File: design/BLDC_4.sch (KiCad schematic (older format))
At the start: 26 parts, among them K1 SERVO, P1 HALL/Encoder, P101 CANBUS, P3 PWR_COMM, P4 IN+, P5 IN-, P6 MOTOR1, P7 MOTOR2, P9 MOTOR3, X1 MINI-USB-SHIELD-32005-201

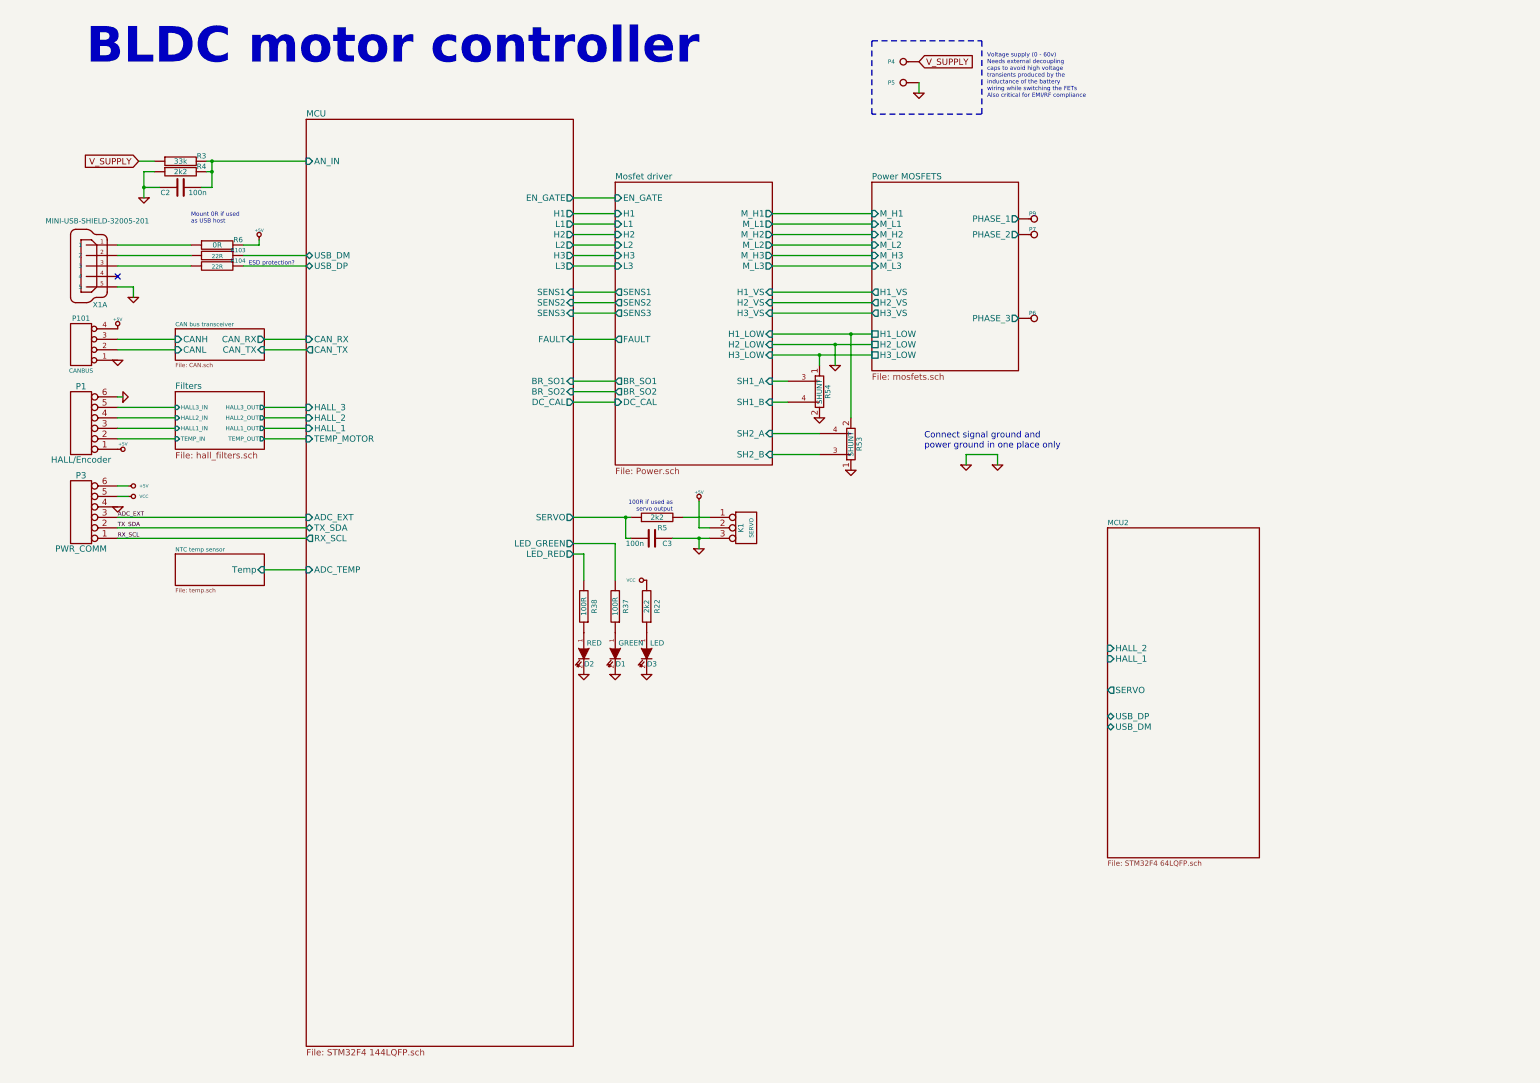
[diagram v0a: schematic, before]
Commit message: Add a electronic for second motor and add new pin's for it on MCU; TODO Add new mosfets
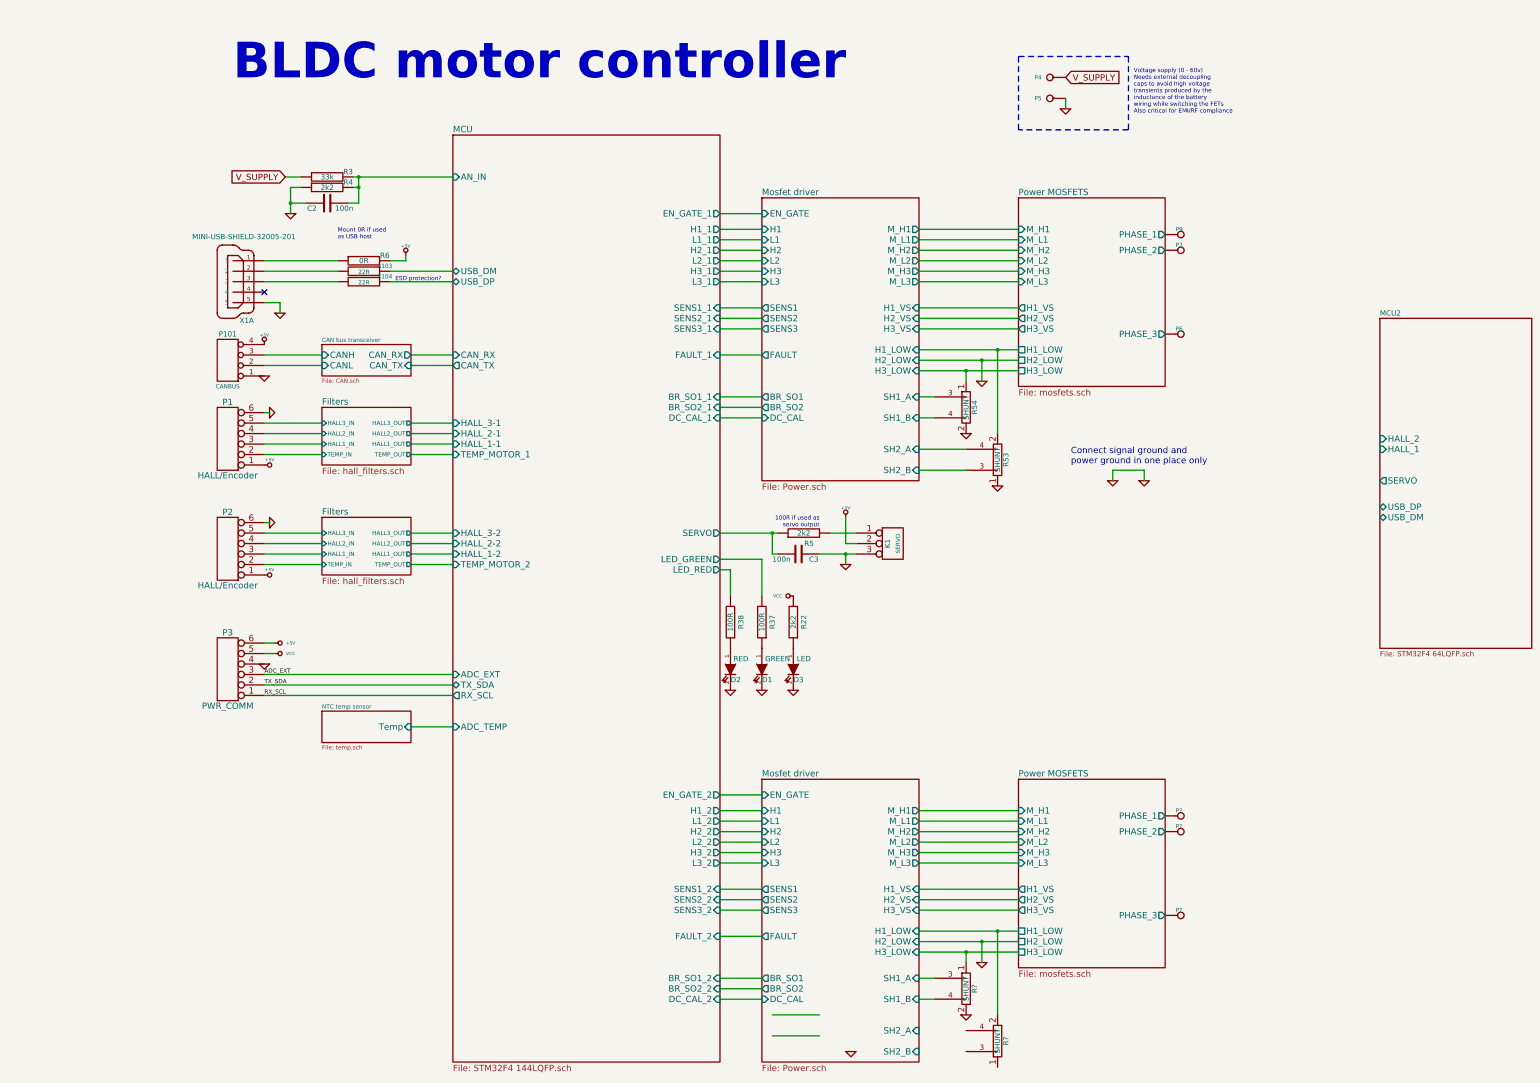
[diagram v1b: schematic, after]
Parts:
- added P2: HALL/Encoder, CRF1:MICRO_JST_6, symbol CONN_6
- added P?: MOTOR3, CRF1:1PAD_4x5mm, symbol CONN_1
- added P?: MOTOR2, CRF1:1PAD_4x5mm, symbol CONN_1
- added P?: MOTOR1, CRF1:1PAD_4x5mm, symbol CONN_1
- added R? (x2): SHUNT, CRF1:WSLP2726, symbol SHUNT
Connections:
- net +5V: now also P2.1
- net Filters/HALL1_IN: now also P2.3; no longer P1.3
- net Filters/HALL2_IN: now also P2.4; no longer P1.4
- net Filters/HALL3_IN: now also P2.5; no longer P1.5
- net Filters/TEMP_IN: now also P2.2; no longer P1.2
- net GND: now also P2.6, R?.2
- net Mosfet driver/H1_LOW: now also R?.2; no longer R53.2
- net Mosfet driver/H3_LOW: now also R?.1; no longer R54.1
- net Mosfet driver/SH1_A: now also R?.3; no longer R54.3
- net Mosfet driver/SH1_B: now also R?.4; no longer R54.4
- net Power MOSFETS/PHASE_1: now also P?.1; no longer P9.1
- net Power MOSFETS/PHASE_2: now also P?.1; no longer P7.1
- net Power MOSFETS/PHASE_3: now also P?.1; no longer P6.1
- new net Filters/HALL1_IN: P1.3
- new net Filters/HALL2_IN: P1.4
- new net Filters/HALL3_IN: P1.5
- new net Filters/TEMP_IN: P1.2
- new net Mosfet driver/H1_LOW: R53.2
- new net Mosfet driver/H3_LOW: R54.1
- new net Mosfet driver/SH1_A: R54.3
- new net Mosfet driver/SH1_B: R54.4
- new net Power MOSFETS/PHASE_1: P9.1
- new net Power MOSFETS/PHASE_2: P7.1
- new net Power MOSFETS/PHASE_3: P6.1
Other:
- moved on the sheet: C2, C3, D1, D2, D3, K1, P1, P101, P3, P4, P5, P6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

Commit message: Make change in annotations and some small fixes
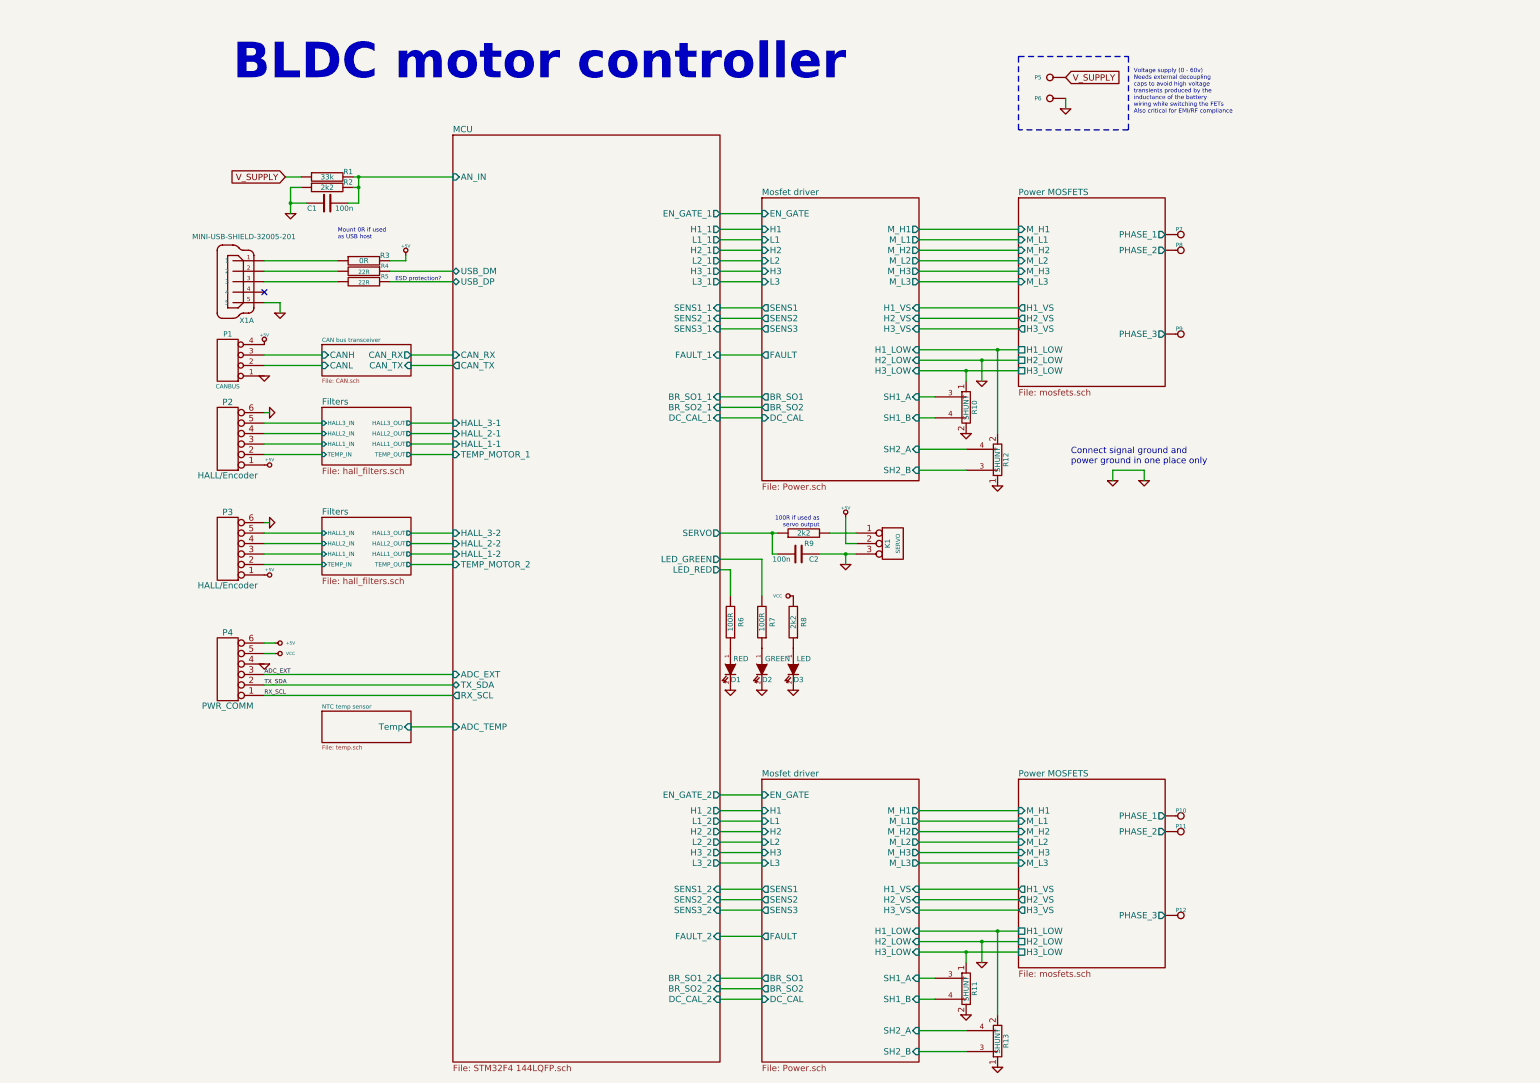
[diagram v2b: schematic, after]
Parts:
- gave numbers to parts that had none: 5
- renumbered C2 to C1, C3 to C2, D2 to D1, D1 to D2, P101 to P1, P1 to P2, P2 to P3, P3 to P4, P4 to P5, P5 to P6, P9 to P7, P7 to P8, P6 to P9, R3 to R1, R54 to R10, R53 to R12, R4 to R2, R6 to R3, R103 to R4, R104 to R5, R38 to R6, R37 to R7, R22 to R8, R5 to R9
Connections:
- net Filters/HALL1_IN is gone; now on net Filters/HALL1_IN: P3.3
- net Filters/HALL2_IN is gone; now on net Filters/HALL2_IN: P3.4
- net Filters/HALL3_IN is gone; now on net Filters/HALL3_IN: P3.5
- net Filters/TEMP_IN is gone; now on net Filters/TEMP_IN: P3.2
- net Mosfet driver/H1_LOW is gone; now on net Mosfet driver/H1_LOW: R13.2
- net Mosfet driver/H3_LOW is gone; now on net Mosfet driver/H3_LOW: R11.1
- net Mosfet driver/SH1_A is gone; now on net Mosfet driver/SH1_A: R11.3
- net Mosfet driver/SH1_B is gone; now on net Mosfet driver/SH1_B: R11.4
- net Power MOSFETS/PHASE_1 is gone; now on net Power MOSFETS/PHASE_1: P10.1
- net Power MOSFETS/PHASE_2 is gone; now on net Power MOSFETS/PHASE_2: P11.1
- net Power MOSFETS/PHASE_3 is gone; now on net Power MOSFETS/PHASE_3: P12.1
- net Filters/HALL1_IN: no longer P2.3
- net Filters/HALL2_IN: no longer P2.4
- net Filters/HALL3_IN: no longer P2.5
- net Filters/TEMP_IN: no longer P2.2
- net GND: now also R13.1
- net Mosfet driver/H1_LOW: no longer R12.2
- net Mosfet driver/H3_LOW: no longer R10.1
- net Mosfet driver/SH1_A: no longer R10.3
- net Mosfet driver/SH1_B: no longer R10.4
- net Mosfet driver/SH2_A: now also R13.4
- net Mosfet driver/SH2_B: now also R13.3
- net Power MOSFETS/PHASE_1: no longer P7.1
- net Power MOSFETS/PHASE_2: no longer P8.1
- net Power MOSFETS/PHASE_3: no longer P9.1
- new net Filters/HALL1_IN: P2.3
- new net Filters/HALL2_IN: P2.4
- new net Filters/HALL3_IN: P2.5
- new net Filters/TEMP_IN: P2.2
- new net Mosfet driver/H1_LOW: R12.2
- new net Mosfet driver/H3_LOW: R10.1
- new net Mosfet driver/SH1_A: R10.3
- new net Mosfet driver/SH1_B: R10.4
- new net Power MOSFETS/PHASE_1: P7.1
- new net Power MOSFETS/PHASE_2: P8.1
- new net Power MOSFETS/PHASE_3: P9.1
